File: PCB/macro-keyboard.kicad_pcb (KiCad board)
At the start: 2 copper layers, 45 parts, among them J1 AVR-ISP-6, SW1 SW_Push, SW10 SW_Push, SW11 SW_Push, SW12 SW_Push, SW2 SW_Push, SW3 SW_Push, SW4 SW_Push, SW5 SW_Push, SW6 SW_Push, SW7 SW_Push, SW8 SW_Push, SW9 SW_Push, U1 PRTR5V0U2X, U2 ATmega32U4-A, Y1 Crystal_GND24_Small

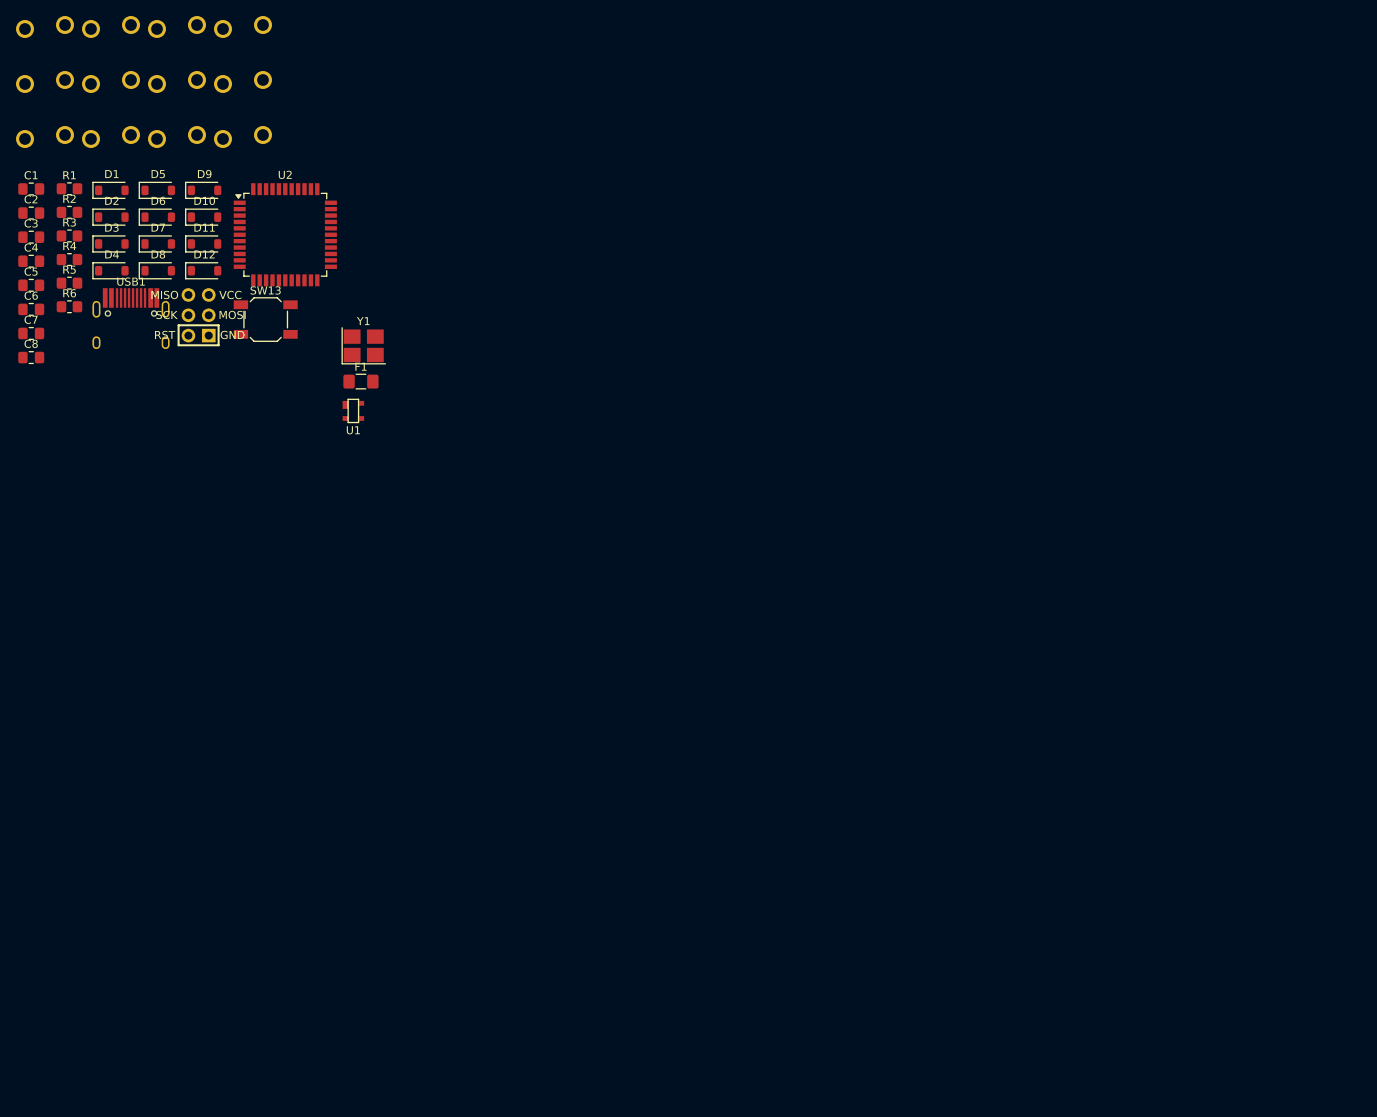
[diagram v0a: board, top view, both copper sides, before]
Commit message: Layout keycaps
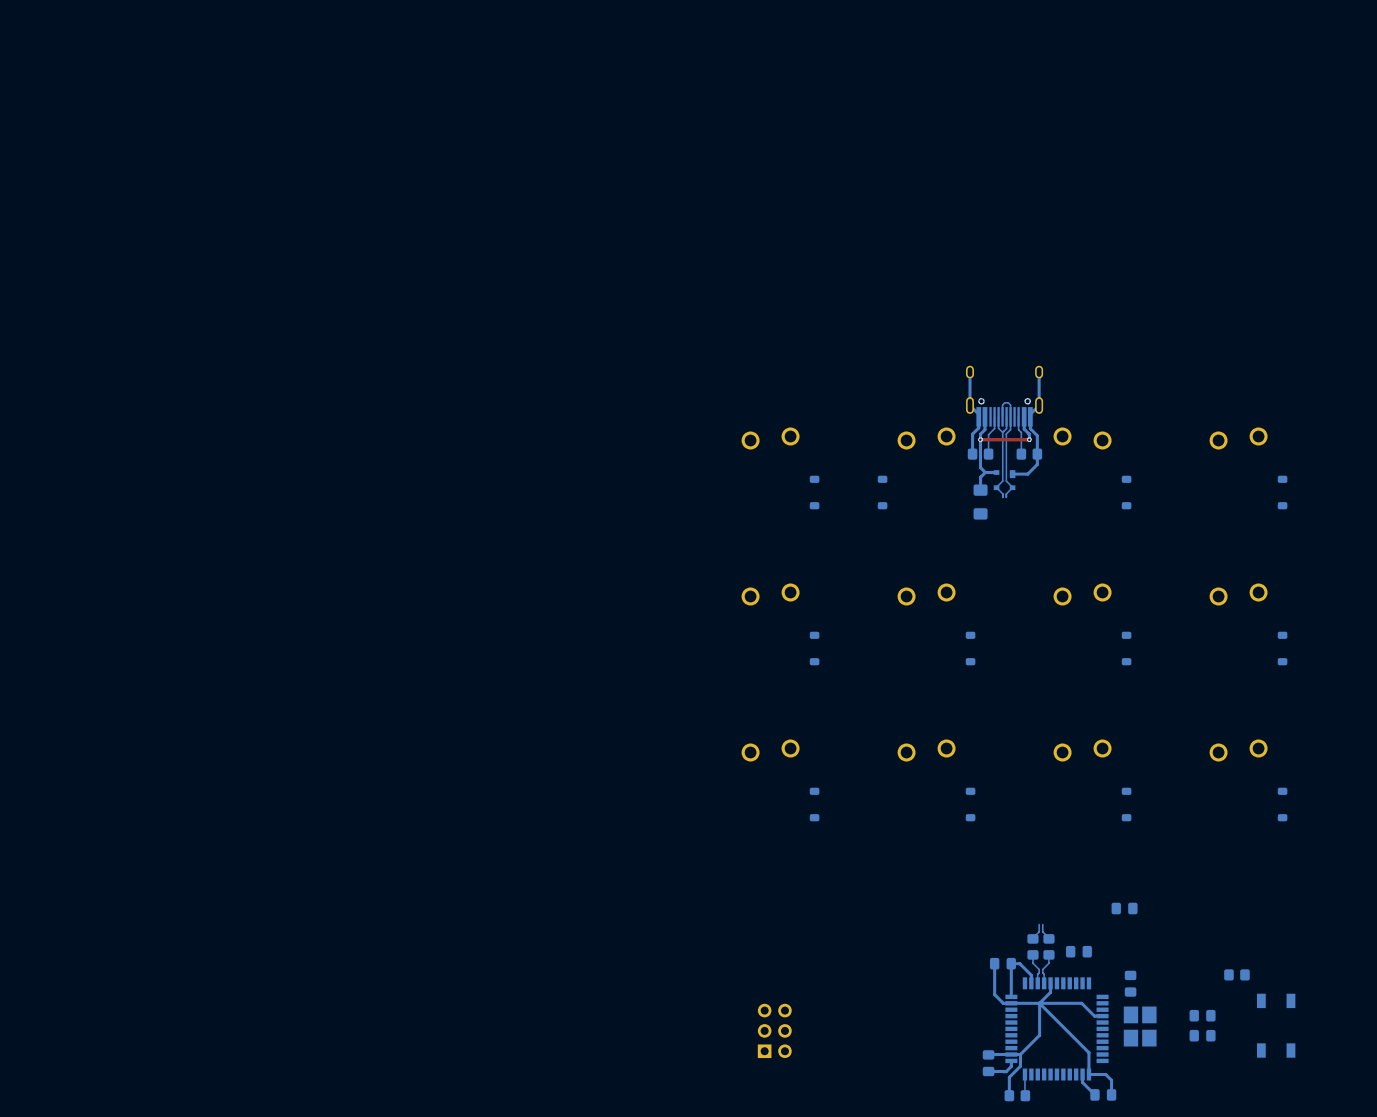
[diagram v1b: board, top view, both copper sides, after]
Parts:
- C1, C2, C3, C4, C5, C6, C7, C8, D1, D10, D11, D12, D2, D3, D4, D5, D6, D7, D8, D9, F1, J1, R1, R2, R3, R4, R5, R6, SW13, SW3, U1, U2, USB1, Y1: moved to B.Cu
- moved C1 179.2 mm to (173.2, 146.8)
- moved C2 178.9 mm to (173.2, 149.3)
- moved C3 171.6 mm to (160.8, 156.7)
- moved R5 169.6 mm to (177.6, 141.7), turned to 180 degrees
- moved C4 164.4 mm to (164.2, 142.8), turned to -90 degrees
- moved C5 154.2 mm to (146.5, 152.7), turned to 90 degrees
- moved R6 154.2 mm to (150.1, 156.8)
- moved SW13 154.1 mm to (182.4, 148.1), turned to -90 degrees
- moved C6 153.6 mm to (157.8, 138.8), turned to 180 degrees
- moved C8 153.0 mm to (163.5, 133.4)
- moved D12 150.4 mm to (183.2, 120.4), turned to 90 degrees
- moved SW4 150.0 mm to (177.8, 78.9)
- moved R3 149.7 mm to (152.1, 138.2), turned to 90 degrees
- moved R4 149.6 mm to (154.1, 138.2), turned to 90 degrees
- moved D4 148.9 mm to (183.2, 81.4), turned to 90 degrees
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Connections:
- net Net-(U1-IO1) renamed DP
- net Net-(U1-IO2) renamed DN
- C1 pad 2: Net-(C1-Pad2) -> GND
- C2 pad 2: Net-(C1-Pad2) -> GND
- D10 pad 1: row0 -> row2
- D11 pad 1: row1 -> row2
- D2 pad 1: row1 -> row0
- D3 pad 1: row2 -> row0
- D6 pad 1: row2 -> row1
- D7 pad 1: row0 -> row1
- SW10 pad 1: col3 -> col1
- SW11 pad 1: col3 -> col2
- SW2 pad 1: col0 -> col1
- SW3 pad 1: col0 -> col2
- SW4 pad 1: col1 -> col3
- SW5 pad 1: col1 -> col0
- SW8 pad 1: col2 -> col3
- SW9 pad 1: col2 -> col0
- Y1 pad 2: Net-(C1-Pad2) -> GND
- Y1 pad 4: Net-(C1-Pad2) -> GND
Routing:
- net GND: track 0.00 -> 82.1 mm
- net VCC: track 0.00 -> 20.5 mm, vias 0 -> 2
- net DP: track 0.00 -> 17.6 mm
- net DN: track 0.00 -> 15.6 mm
- net +5V: track 0.00 -> 15.3 mm
- net Net-(USB1-CC1): track 0.00 -> 4.97 mm
- net Net-(USB1-CC2): track 0.00 -> 4.80 mm
- net D+: track 0.00 -> 3.94 mm
- net D-: track 0.00 -> 3.94 mm
- net Net-(U2-~{HWB}/PE2): track 0.00 -> 2.67 mm

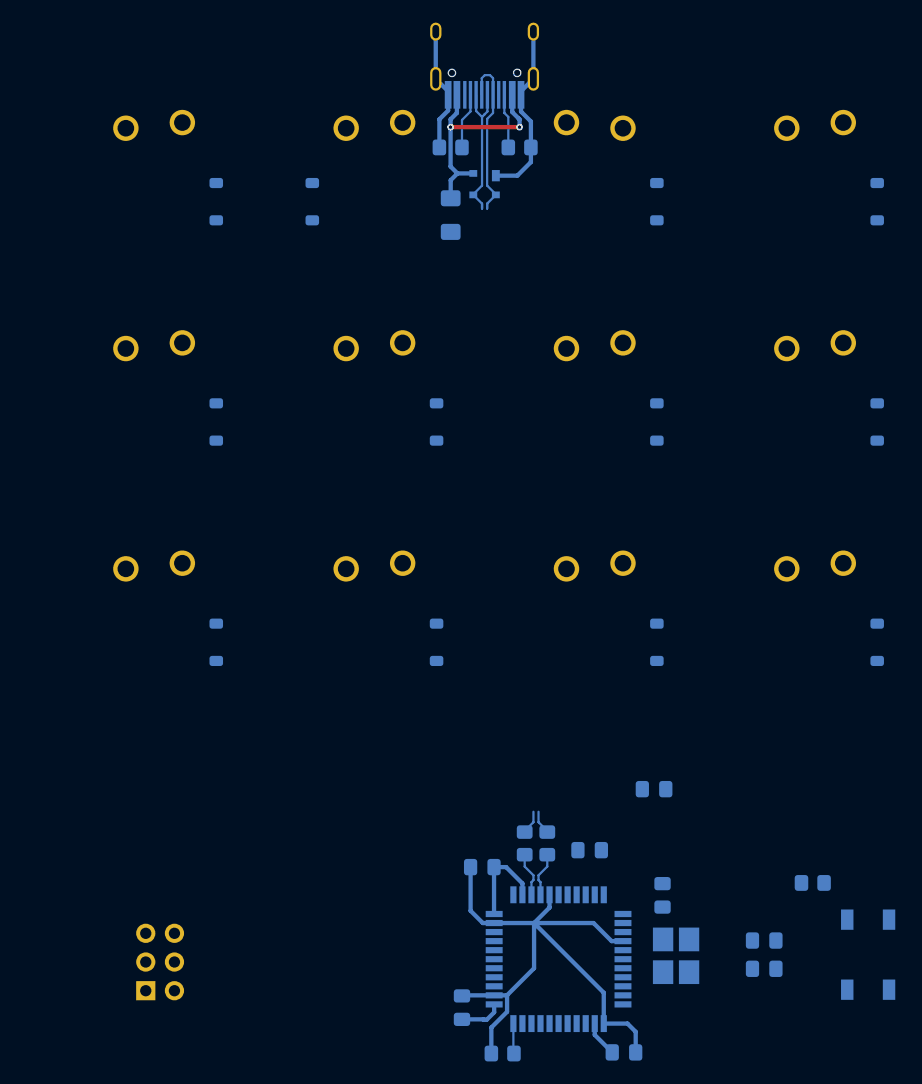
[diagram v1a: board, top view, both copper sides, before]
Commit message: Layout traces and remove isp header and fours keys
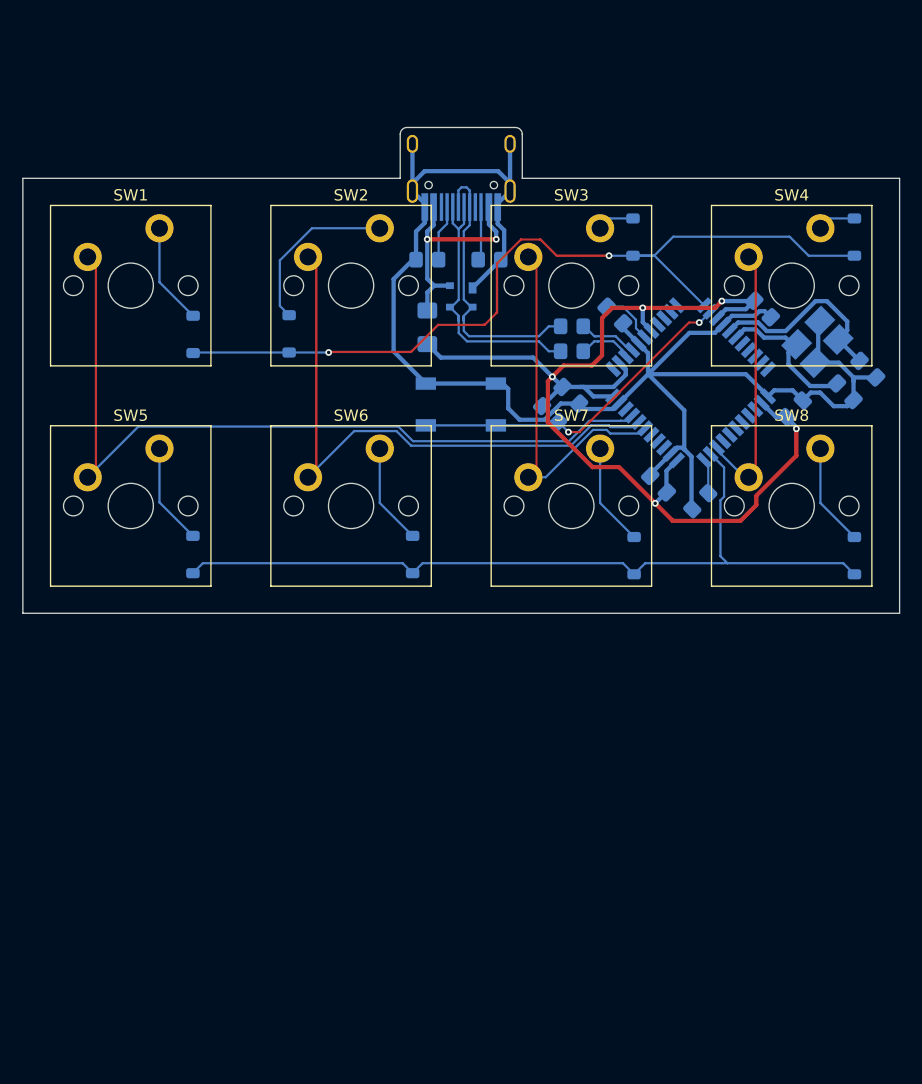
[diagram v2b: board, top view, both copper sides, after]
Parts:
- removed C6: 0.1u, Capacitor_SMD:C_0805_2012Metric_Pad1.18x1.45mm_HandSolder
- removed D10, D11, D12, D9: D, Diode_SMD:D_SOD-123
- removed J1: AVR-ISP-6, random-keyboard-parts:Reset_Pretty-Mask
- removed SW10, SW11, SW12, SW9: SW_Push, Alps_Only:ALPS-1U
- SW1, SW2, SW4, SW5, SW6, SW7, SW8: footprint Alps_Only:ALPS-1U -> ScottoKeebs_MX:MX_PCB_1.00u
- SW3: footprint Alps_Only:ALPS-1U -> ScottoKeebs_MX:MX_PCB_1.00u; moved to F.Cu
- moved SW13 60.6 mm to (146.4, 99.3), turned to 0 degrees
- moved C3 58.9 mm to (175.9, 99.7), turned to 45 degrees
- moved Y1 55.8 mm to (178.0, 93.8), turned to 45 degrees
- moved C2 53.9 mm to (182.4, 96.2), turned to -45 degrees
- moved C4 52.6 mm to (173.1, 90.9), turned to -45 degrees
- moved U2 52.3 mm to (166.7, 97.4), turned to -45 degrees
- moved R6 51.9 mm to (167.6, 107.9), turned to 45 degrees
- moved C5 49.5 mm to (163.9, 106.4), turned to 135 degrees
- moved C1 49.1 mm to (180.4, 98.2), turned to -45 degrees
- moved R5 47.6 mm to (154.3, 100.2), turned to 135 degrees
- moved R4 45.8 mm to (156.2, 92.4), turned to 180 degrees
- moved R3 43.8 mm to (156.2, 94.6), turned to 180 degrees
- moved C7 42.5 mm to (156.1, 98.5), turned to -45 degrees
- moved C8 42.1 mm to (160.0, 91.4), turned to -45 degrees
- moved D7 12.0 mm to (161.7, 112.7)
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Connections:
- U2 pad 10: MOSI -> unconnected-(U2-PB2-Pad10)
- U2 pad 11: MISO -> unconnected-(U2-PB3-Pad11)
- U2 pad 12: unconnected-(U2-PB7-Pad12) -> row0
- U2 pad 28: col0 -> unconnected-(U2-PB4-Pad28)
- U2 pad 29: col1 -> unconnected-(U2-PB5-Pad29)
- U2 pad 30: col2 -> unconnected-(U2-PB6-Pad30)
- U2 pad 32: unconnected-(U2-PC7-Pad32) -> row1
- U2 pad 39: row2 -> col2
- U2 pad 40: row1 -> col1
- U2 pad 41: row0 -> col0
- U2 pad 9: SCK -> unconnected-(U2-PB1-Pad9)
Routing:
- net +5V: track 15.3 -> 99.4 mm, vias 0 -> 5
- net row0: track 0.00 -> 75.4 mm, vias 0 -> 2
- net col0: track 0.00 -> 71.6 mm
- net row1: track 0.00 -> 71.4 mm
- net GND: track 82.1 -> 142.7 mm
- net col1: track 0.00 -> 52.6 mm
- net col2: track 0.00 -> 32.5 mm
- net RESET: track 0.00 -> 30.1 mm, vias 0 -> 2
- net col3: track 0.00 -> 24.0 mm
- net XTAL2: track 0.00 -> 17.5 mm
- net Net-(D2-A): track 0.00 -> 15.2 mm
- net XTAL1: track 0.00 -> 13.5 mm
- net DN: track 15.6 -> 24.8 mm
- net Net-(D8-A): track 0.00 -> 9.08 mm
- net Net-(D7-A): track 0.00 -> 9.08 mm
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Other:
- board outline added: 77.6 x 43 mm

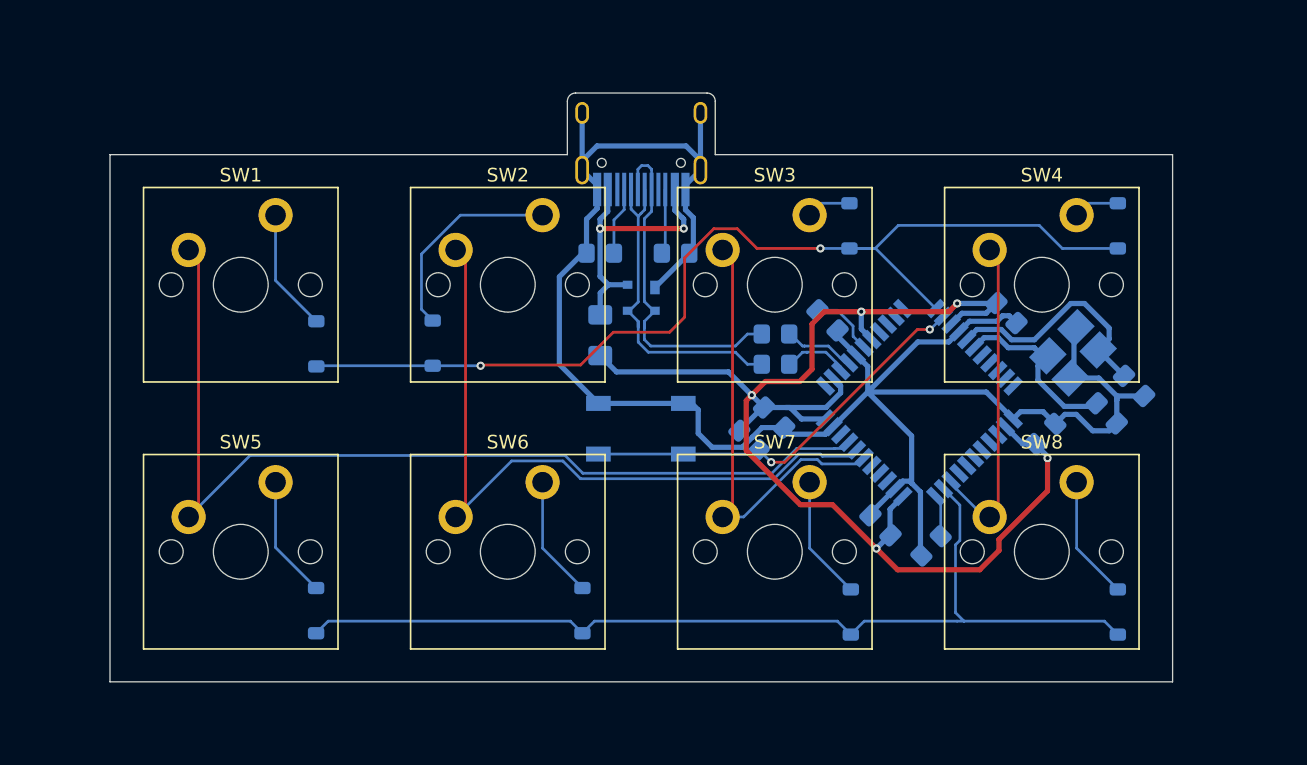
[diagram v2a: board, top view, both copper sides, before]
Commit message: Update models and add mounting holes
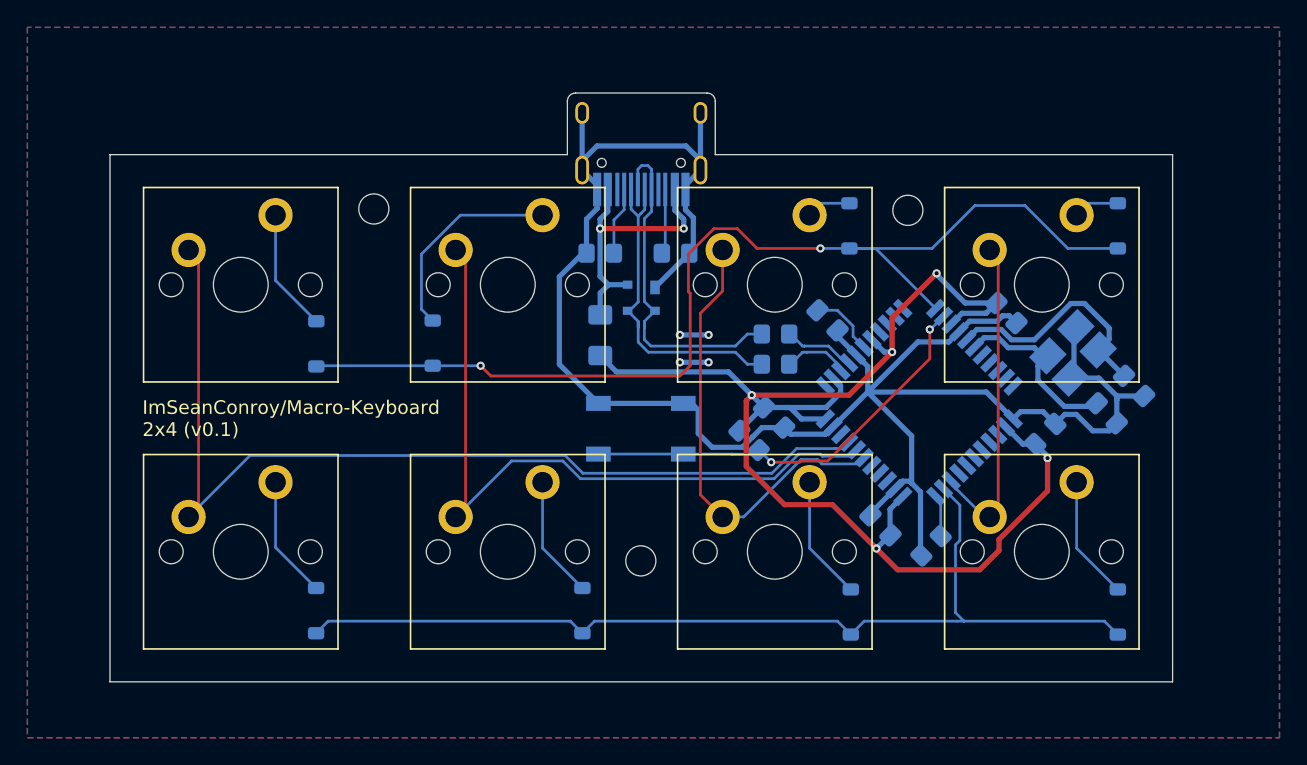
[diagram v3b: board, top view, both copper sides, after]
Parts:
- added REF**: MountingHole_2.2mm_M2_DIN965, MountingHole:MountingHole_2.2mm_M2_DIN965, F.Cu at (146.4, 109.0)
- added REF**: MountingHole_2.2mm_M2_DIN965, MountingHole:MountingHole_2.2mm_M2_DIN965, F.Cu at (165.9, 83.4)
- added REF**: MountingHole_2.2mm_M2_DIN965, MountingHole:MountingHole_2.2mm_M2_DIN965, F.Cu at (126.9, 83.3)
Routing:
- net row0: track 75.4 -> 79.6 mm
- net GND: track 142.7 -> 146.9 mm, vias 0 -> 4
- net +5V: track 99.4 -> 100.9 mm
- net RESET: track 30.1 -> 31.4 mm
- net col2: track 32.5 -> 33.2 mm
- added copper zone on B.Cu, net GND
- added copper zone on F.Cu, net GND
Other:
- board text added: "ImSeanConroy/Macro-Keyboard 2x4 (v0.1)"
